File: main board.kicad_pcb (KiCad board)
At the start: 2 copper layers, 159 x 146 mm, 88 parts, among them J1 #15, J10 #11, J11 #14, J12 #37, J13 #3, J14 #23, J15 #33, J16 #38, J17 #4, J18 #13, J19 #9, J2 Red-Blk, J20 #18, J21 #22, J22 #21, J23 #25, J24 #8, J25 #16, J26 #12, J27 #35, J28 #7, J29 #19, J3 #2, J30 #26, J31 #5, J32 #28, J33 #32, J34 #39, J35 #27, J36 #40, J37 #17, J38 #20, J39 #24, J4 Blk, J40 #29, J41 #30, J42 #31, J43 #34, J44 #36, J45 #Brn, J46 #Blu, J47 #L2, J48 #L1, J5 #1, J6 #6, J7 #10, J8 Red-Yel, J9 Red-Grn, U1 6AL5, U2 ECC83

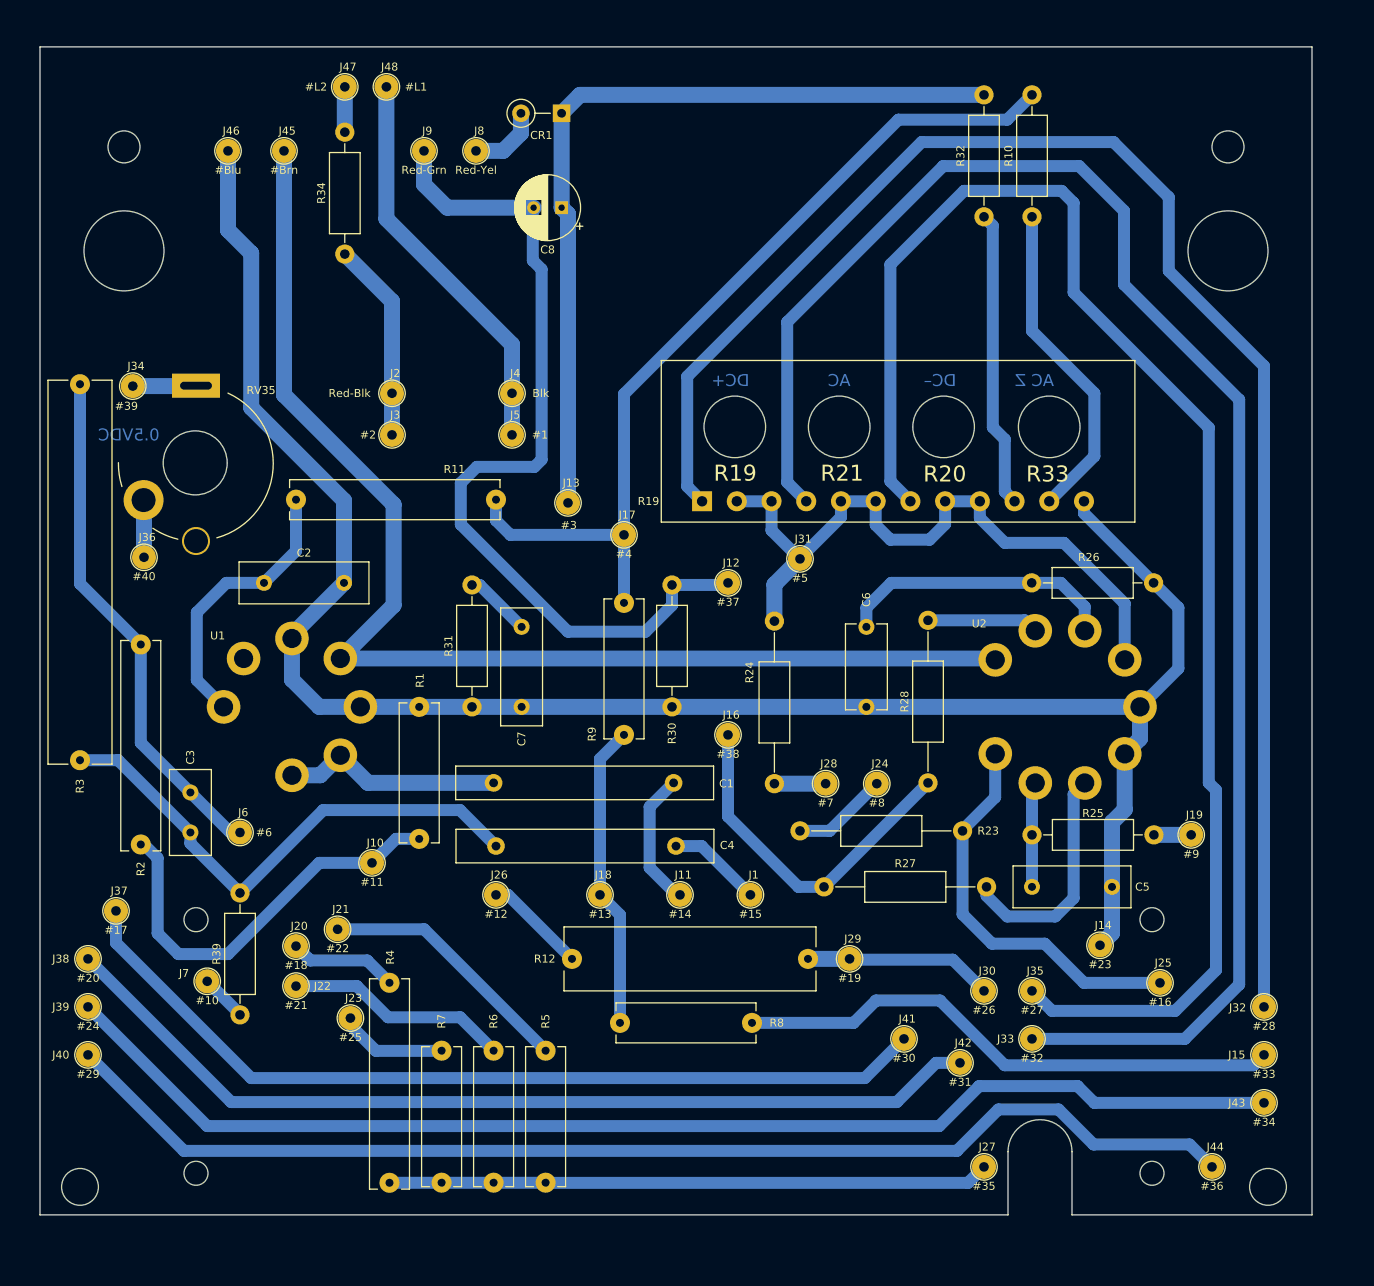
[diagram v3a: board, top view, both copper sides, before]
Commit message: 2 side layout with bottom gound plane
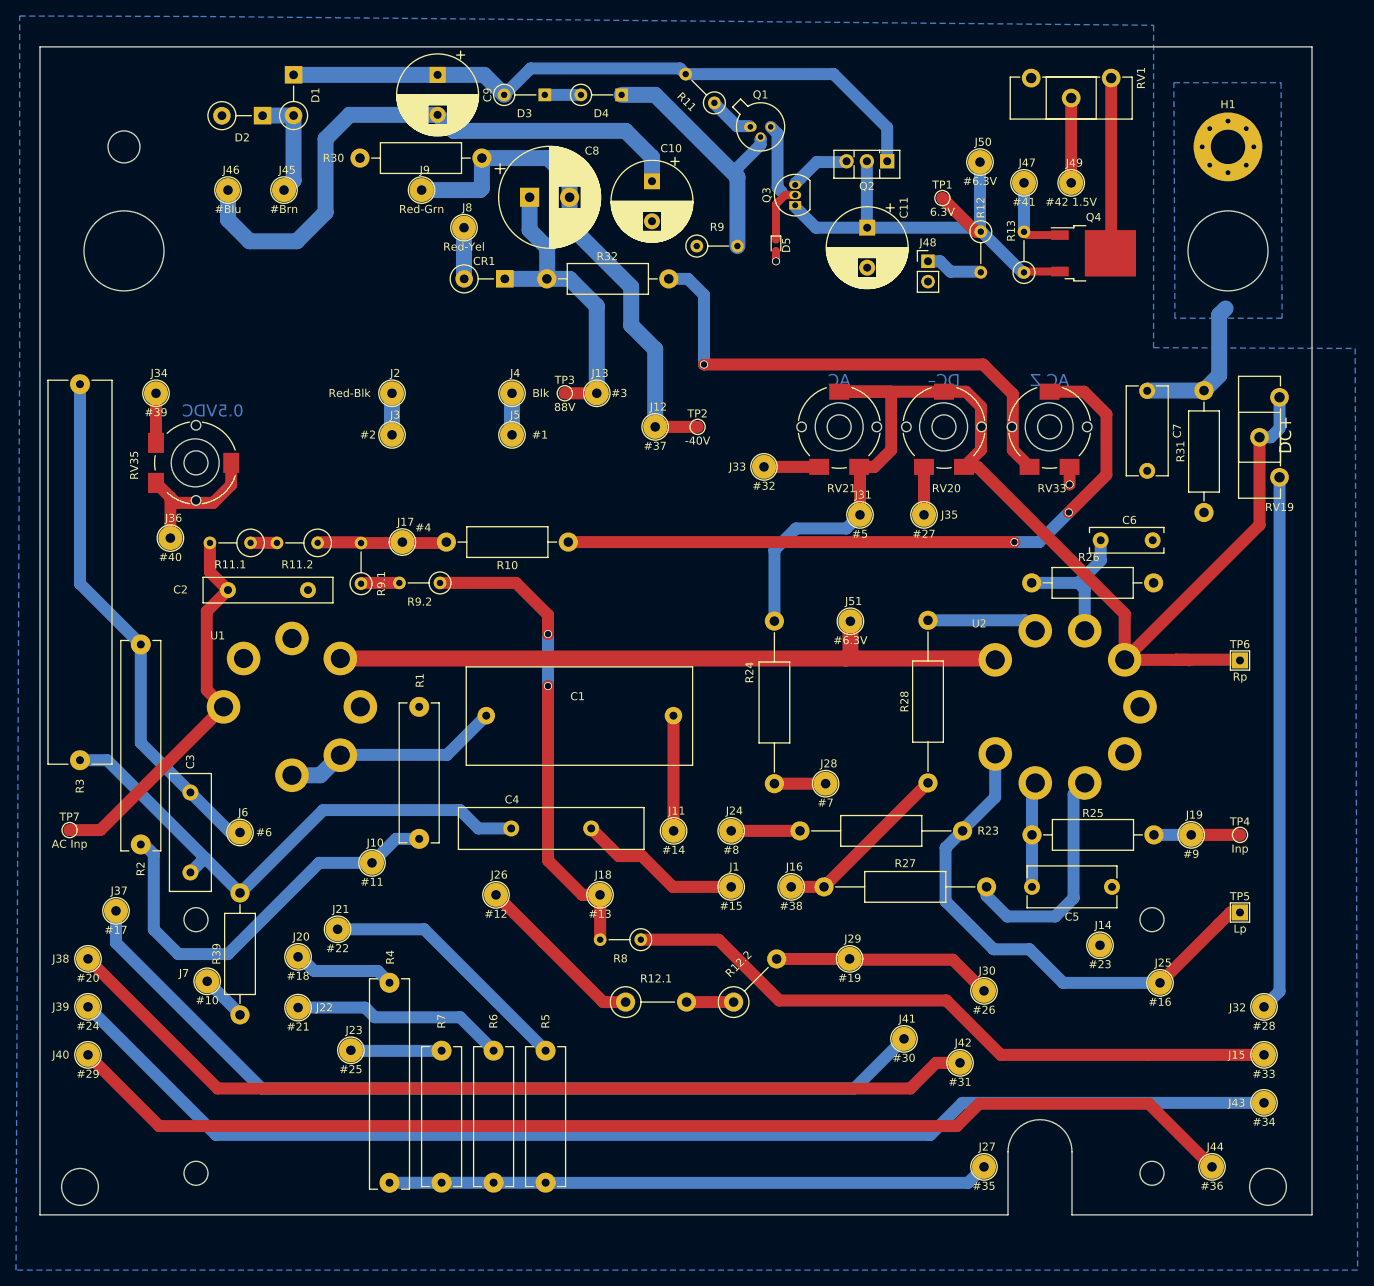
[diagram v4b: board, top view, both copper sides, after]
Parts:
- removed ? (x4): , 
- removed R19: R-4, wv98:R-4-in-row
- removed R34: 180k, Resistor_THT:R_Axial_DIN0411_L9.9mm_D3.6mm_P15.24mm_Horizontal
- added C10: 1000uF, Capacitor_THT:CP_Radial_D10.0mm_P5.00mm, F.Cu at (171.3, 79.1)
- added C11: 1000uF, Capacitor_THT:CP_Radial_D10.0mm_P5.00mm, F.Cu at (198.2, 84.9)
- added C9: 1000uF, Capacitor_THT:CP_Radial_D10.0mm_P5.00mm, F.Cu at (144.5, 65.8)
- added D1: 1N4001, Diode_THT:D_DO-41_SOD81_P5.08mm_Vertical_KathodeUp, F.Cu at (126.5, 65.8)
- added D2: 1N4001, Diode_THT:D_DO-41_SOD81_P5.08mm_Vertical_KathodeUp, F.Cu at (122.6, 70.9)
- added D3: 1N4148, Diode_THT:D_DO-35_SOD27_P5.08mm_Vertical_KathodeUp, F.Cu at (157.9, 68.3)
- added D4: 1N4148, Diode_THT:D_DO-35_SOD27_P5.08mm_Vertical_KathodeUp, F.Cu at (167.5, 68.3)
- added D5: 6V9, Diode_SMD:D_SOD-523, F.Cu at (186.8, 87.1)
- added H1: MountingHole, MountingHole:MountingHole_4.3mm_M4_Pad_Via, F.Cu at (243.3, 74.8)
- added J49: #42 1.5V, wv98:Hole_Din1.2mm_Dout3mm, F.Cu at (223.7, 79.3)
- added J50: #6.3V, wv98:Hole_Din1.2mm_Dout3mm, F.Cu at (212.3, 76.7)
- added J51: #6.3V, wv98:Hole_Din1.2mm_Dout3mm, F.Cu at (196.1, 134.1)
- added Q1: 2N2907, Package_TO_SOT_THT:TO-18-3, F.Cu at (183.6, 72.3)
- added Q2: BD136, Package_TO_SOT_THT:TO-126-3_Vertical, F.Cu at (200.7, 76.6)
- added Q3: PN2222A, Package_TO_SOT_THT:TO-92_Inline, F.Cu at (189.2, 82.1)
- added Q4: DMP4010SK3Q, Package_TO_SOT_SMD:TO-252-2, F.Cu at (226.5, 88.1)
- added R11: 100, Resistor_THT:R_Axial_DIN0207_L6.3mm_D2.5mm_P5.08mm_Vertical, F.Cu at (179.1, 69.3)
- added R11.2: 1M, Resistor_THT:R_Axial_DIN0309_L9.0mm_D3.2mm_P5.08mm_Vertical, F.Cu at (129.5, 124.3)
- added R12: 330, Resistor_THT:R_Axial_DIN0207_L6.3mm_D2.5mm_P5.08mm_Vertical, F.Cu at (212.4, 85.4)
- added R12.1: 2M, Resistor_THT:R_Axial_DIN0411_L9.9mm_D3.6mm_P7.62mm_Vertical, F.Cu at (168.0, 181.7)
- added R13: 10k, Resistor_THT:R_Axial_DIN0207_L6.3mm_D2.5mm_P5.08mm_Vertical, F.Cu at (217.8, 90.5)
- added R9: 20k, Resistor_THT:R_Axial_DIN0207_L6.3mm_D2.5mm_P5.08mm_Vertical, F.Cu at (176.9, 87.2)
- added R9.2: 40.2k, Resistor_THT:R_Axial_DIN0207_L6.3mm_D2.5mm_P5.08mm_Vertical, F.Cu at (144.8, 129.3)
- added RV1: 10k, Potentiometer_THT:Potentiometer_Piher_PT-15-H01_Horizontal, F.Cu at (228.7, 66.2)
- added RV19: R_POT, Potentiometer_THT:Potentiometer_Piher_PT-15-H01_Horizontal, F.Cu at (249.7, 116.1)
- added RV20: R_POT, Potentiometer_SMD:Potentiometer_Piher_PS_PSX-10-V60_Vertical, F.Cu at (207.8, 110.1)
- added RV21: R_POT, Potentiometer_SMD:Potentiometer_Piher_PS_PSX-10-V60_Vertical, F.Cu at (194.7, 110.1)
- added RV33: R_POT, Potentiometer_SMD:Potentiometer_Piher_PS_PSX-10-V60_Vertical, F.Cu at (221.0, 110.1)
- added TP1: 6.3V, TestPoint:TestPoint_Pad_D1.5mm, F.Cu at (207.6, 81.2)
- added TP2: -40V, TestPoint:TestPoint_Pad_D1.5mm, F.Cu at (177.0, 109.8)
- added TP3: 88V, TestPoint:TestPoint_Pad_D1.5mm, F.Cu at (160.4, 105.6)
- added TP4: Inp, TestPoint:TestPoint_Pad_D1.5mm, F.Cu at (244.8, 160.8)
- added TP5: Lp, TestPoint:TestPoint_THTPad_2.0x2.0mm_Drill1.0mm, F.Cu at (244.8, 170.5)
- added TP6: Rp, TestPoint:TestPoint_THTPad_2.0x2.0mm_Drill1.0mm, F.Cu at (244.8, 139.0)
- added TP7: AC Inp, TestPoint:TestPoint_Pad_D1.5mm, F.Cu at (98.5, 160.2)
- C1: footprint wv98:С1 -> wv98:6PSS50
- C2: footprint Capacitor_THT:C_Disc_D16.0mm_W5.0mm_P10.00mm -> wv98:562R5GAS20-C2
- C3: footprint Capacitor_THT:C_Disc_D10.5mm_W5.0mm_P5.00mm -> Capacitor_THT:C_Disc_D14.5mm_W5.0mm_P10.00mm
- C4: footprint wv98:С1 -> wv98:562R20GAP10-C4
- C5, C7: footprint Capacitor_THT:C_Disc_D14.5mm_W5.0mm_P10.00mm -> Capacitor_THT:C_Disc_D11.0mm_W5.0mm_P10.00mm
- C6: footprint Capacitor_THT:C_Disc_D10.5mm_W5.0mm_P10.00mm -> wv98:S502M39Z5UN-C6
- C8: footprint Capacitor_THT:CP_Radial_D8.0mm_P3.50mm -> Capacitor_THT:CP_Radial_D12.5mm_P5.00mm
- J47: value #L2 -> #41
- J48: value #L1 -> LED conn; footprint wv98:Hole_Din1.2mm_Dout3mm -> Connector_PinHeader_2.54mm:PinHeader_1x02_P2.54mm_Vertical
- R11.1: renamed from R11; value 16M -> 15M; footprint wv98:R2 -> Resistor_THT:R_Axial_DIN0309_L9.0mm_D3.2mm_P5.08mm_Vertical
- R12.2: renamed from R12; value 7M -> 5M; footprint wv98:R12 -> Resistor_THT:R_Axial_DIN0411_L9.9mm_D3.6mm_P7.62mm_Vertical
- R8: footprint wv98:R1-like -> Resistor_THT:R_Axial_DIN0207_L6.3mm_D2.5mm_P5.08mm_Vertical
- R9.1: renamed from R9; value 8.49M -> 8.45M; footprint wv98:R1-like -> Resistor_THT:R_Axial_DIN0207_L6.3mm_D2.5mm_P5.08mm_Vertical
- RV35: footprint wv98:R35 -> Potentiometer_SMD:Potentiometer_Piher_PS_PSX-10-V60_Vertical
- moved R31 94.7 mm to (240.3, 120.5)
- moved J47 85.7 mm to (217.8, 79.3)
- moved C7 83.6 mm to (233.2, 105.3)
- moved J33 79.0 mm to (185.3, 114.8)
- moved R30 78.9 mm to (134.8, 76.2), turned to 0 degrees
- moved J48 71.1 mm to (205.8, 89.1)
- moved R10 70.8 mm to (160.8, 124.2), turned to 180 degrees
- moved J35 61.0 mm to (205.3, 120.8)
- moved R32 40.2 mm to (173.4, 91.3), turned to 180 degrees
- moved R9.1 37.9 mm to (134.9, 129.4)
- moved C6 31.2 mm to (227.4, 124.0), turned to 0 degrees
- moved R11.1 31.1 mm to (121.1, 124.3)
- moved J17 27.7 mm to (140.1, 124.2)
- moved CR1 21.9 mm to (152.9, 91.3)
- moved J12 21.5 mm to (171.7, 109.8)
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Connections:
- net GNDREF renamed Earth
- net R34 renamed Net-(J2-Pad1)
- J45 pad 1: Net-(J45-Pad1) -> Net-(D1-Pad2)
- J46 pad 1: GND -> Net-(C10-Pad1)
- J48 pad 1: Net-(J4-Pad1) -> Net-(J48-Pad1)
- R11.1 pad 1: Net-(J17-Pad1) -> Net-(R11.1-Pad1)
- R12.2 pad 1: Net-(J26-Pad1) -> Net-(R12.1-Pad2)
- R9.1 pad 1: Net-(J18-Pad1) -> Net-(R9.1-Pad1)
- RV35 pad 3: (no net) -> Net-(J36-Pad1)
- U1 pad 4: Net-(J45-Pad1) -> Net-(J51-Pad1)
- U2 pad 9: Net-(J45-Pad1) -> Net-(J51-Pad1)
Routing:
- net GND: track 246.7 -> 3.64 mm, vias 0 -> 2
- net Net-(J33-Pad1): track 207.3 -> 6.90 mm
- net Net-(J35-Pad1): track 187.4 -> 6.00 mm
- net Net-(J45-Pad1): track 153.8 -> 0.00 mm
- net Net-(J32-Pad1): track 197.7 -> 67.0 mm
- net Net-(J17-Pad1): track 111.9 -> 16.2 mm
- net Net-(J51-Pad1): track 0.00 -> 86.8 mm
- net Net-(C9-Pad1): track 0.00 -> 83.9 mm
- net Net-(J31-Pad1): track 87.8 -> 164.3 mm
- net Net-(C10-Pad1): track 0.00 -> 74.9 mm
- net Net-(C8-Pad1): track 102.8 -> 38.9 mm
- net Net-(C11-Pad1): track 0.00 -> 60.1 mm
- net Net-(C8-Pad2): track 110.6 -> 64.1 mm
- net Net-(R10-Pad1): track 41.1 -> 86.6 mm, vias 0 -> 2
- net Net-(J4-Pad1): track 50.0 -> 5.20 mm
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- added copper zone on B.Cu, net Earth
- added copper zone on B.Cu, net GND
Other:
- outline, holes or cut-outs redrawn
- net class Default: clearance 0.5 -> 0.2
- rule trace_clearance: 0.5 -> 0.2
- rule trace_min: 1.5 -> 1

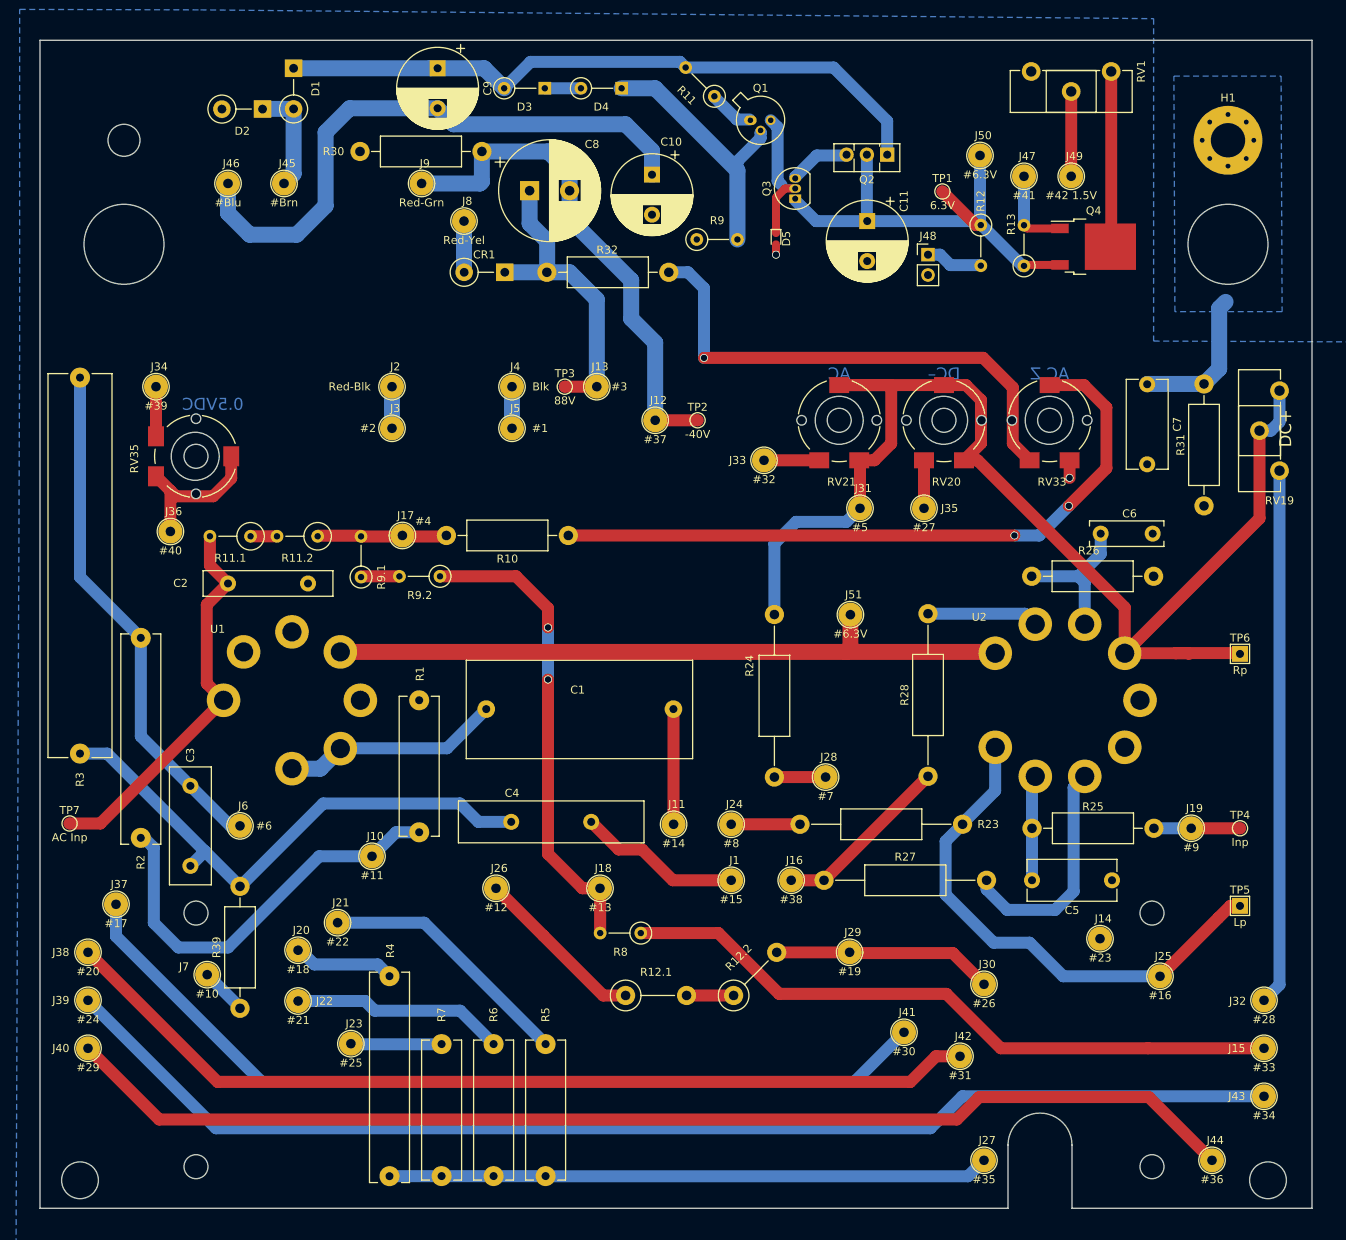
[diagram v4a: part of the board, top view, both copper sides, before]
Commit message: Add heatsink for main BJT
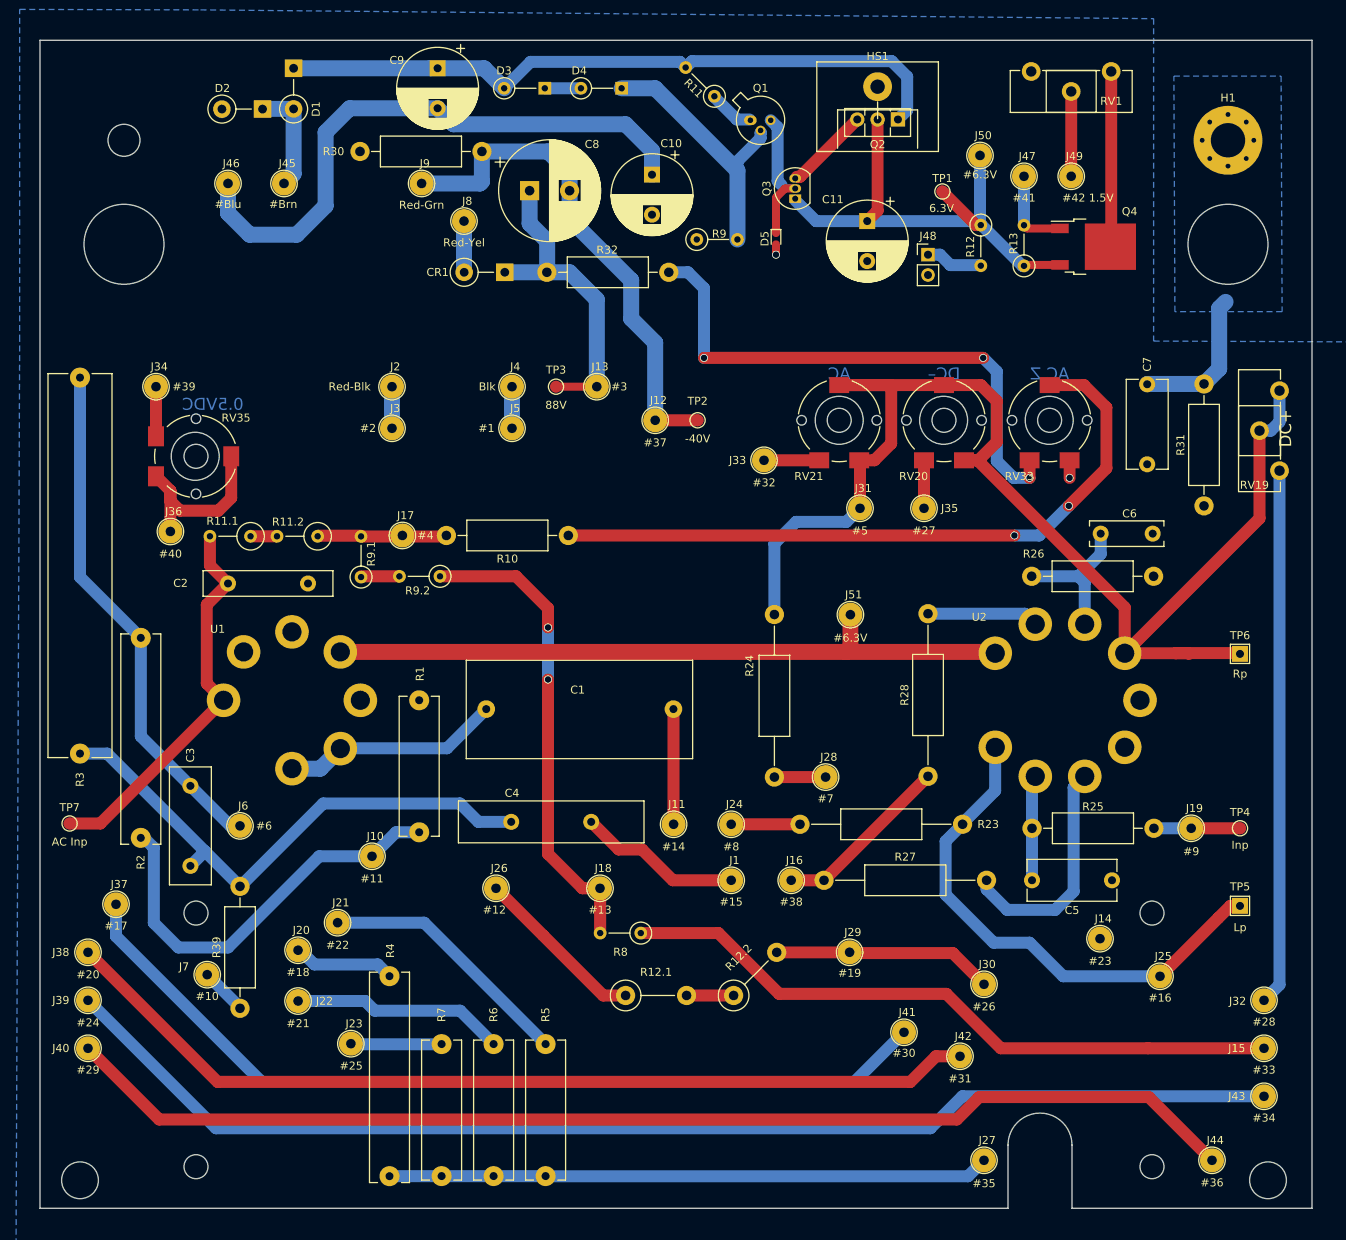
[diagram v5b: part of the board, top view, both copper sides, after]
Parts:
- added HS1: Heatsink, wv98:heatsink, F.Cu at (199.5, 68.1)
- moved Q2 4.60 mm to (202.0, 72.2)
- moved TP3 1.10 mm to (159.3, 105.6)
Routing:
- net Net-(R32-Pad1): track 64.0 -> 69.6 mm, vias 1 -> 3
- net Net-(C11-Pad1): track 60.1 -> 65.1 mm
- net Net-(J31-Pad1): track 164.3 -> 168.1 mm
- net Net-(J36-Pad1): track 19.2 -> 22.9 mm
- net Net-(Q2-Pad3): track 7.55 -> 10.5 mm
- net Net-(C9-Pad1): track 83.9 -> 86.4 mm
- net Net-(C8-Pad1): track 38.9 -> 40.0 mm
